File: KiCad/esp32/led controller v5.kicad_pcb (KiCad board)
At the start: 2 copper layers, 100 x 100 mm, 119 parts, among them J1 Conn_02x15_Counter_Clockwise, J10 Jack-DC, J13 i2c_3.3v, J2 charger, J3 Screw_Terminal_01x09, J4 Screw_Terminal_01x04, J5 Screw_Terminal_01x08, J6 OLED, J7 inverter, J8 i2c_5v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

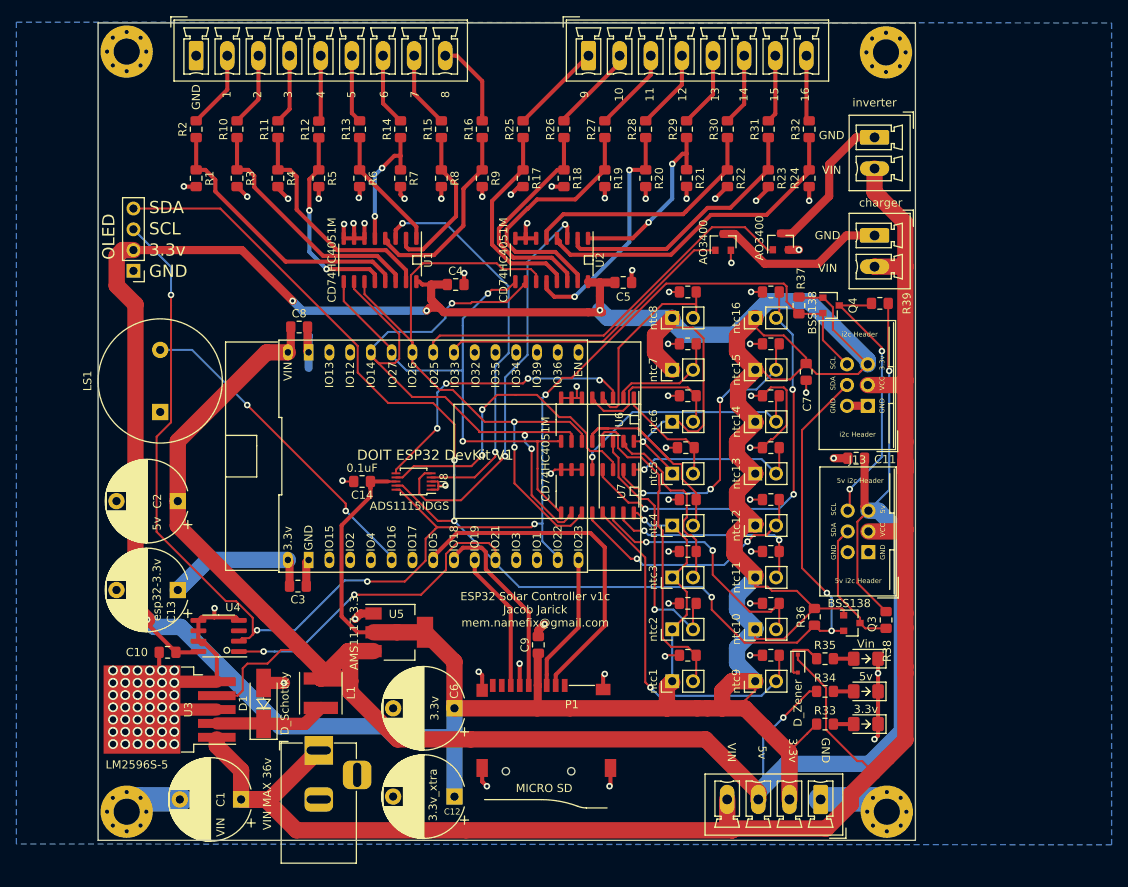
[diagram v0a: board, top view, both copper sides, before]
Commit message: updated ESP32 board
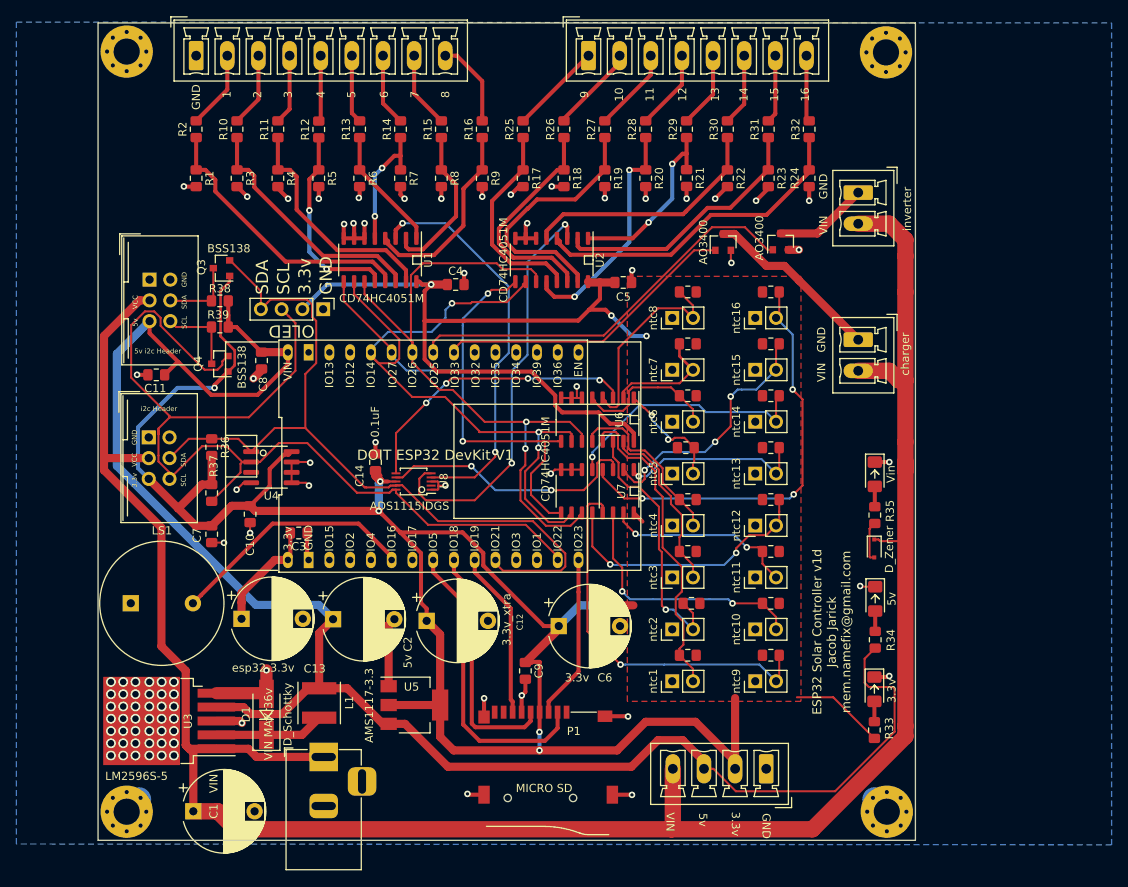
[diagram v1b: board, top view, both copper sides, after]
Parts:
- moved J8 94.1 mm to (7.30, 40.4), turned to 0 degrees
- moved R38 90.4 mm to (15.9, 43.0), turned to 0 degrees
- moved Q3 88.5 mm to (16.1, 39.0), turned to 180 degrees
- moved J13 88.1 mm to (7.20, 59.7), turned to 0 degrees
- moved C11 86.2 mm to (8.12, 52.0)
- moved R39 80.8 mm to (15.9, 46.2)
- moved R36 76.6 mm to (14.9, 60.9), turned to 270 degrees
- moved R37 75.4 mm to (14.9, 66.5)
- moved C7 75.4 mm to (14.9, 71.5)
- moved Q4 75.1 mm to (15.9, 50.7), turned to 180 degrees
- moved C2 23.9 mm to (29.8, 82.0), turned to 0 degrees
- moved J6 23.7 mm to (28.5, 44.0), turned to 270 degrees
- moved LS1 23.7 mm to (5.00, 80.0), turned to 0 degrees
- moved D5 22.6 mm to (96.0, 64.2), turned to 270 degrees
- moved C12 21.8 mm to (41.2, 82.2), turned to 0 degrees
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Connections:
- R40 pad 1: GND -> +3V3
- R41 pad 1: GND -> +3V3
- R42 pad 1: GND -> +3V3
- R43 pad 1: GND -> +3V3
- R44 pad 1: GND -> +3V3
- R45 pad 1: GND -> +3V3
- R46 pad 1: GND -> +3V3
- R47 pad 1: GND -> +3V3
- R48 pad 1: GND -> +3V3
- R49 pad 1: GND -> +3V3
- R50 pad 1: GND -> +3V3
- R51 pad 1: GND -> +3V3
- R52 pad 1: GND -> +3V3
- R53 pad 1: GND -> +3V3
- R54 pad 1: GND -> +3V3
- R55 pad 1: GND -> +3V3
- ntc1 pad 1: +3V3 -> GND
- ntc10 pad 1: +3V3 -> GND
- ntc11 pad 1: +3V3 -> GND
- ntc12 pad 1: +3V3 -> GND
- ntc13 pad 1: +3V3 -> GND
- ntc14 pad 1: +3V3 -> GND
- ntc15 pad 1: +3V3 -> GND
- ntc16 pad 1: +3V3 -> GND
- ntc2 pad 1: +3V3 -> GND
- ntc3 pad 1: +3V3 -> GND
- ntc4 pad 1: +3V3 -> GND
- ntc5 pad 1: +3V3 -> GND
- ntc6 pad 1: +3V3 -> GND
- ntc7 pad 1: +3V3 -> GND
- ntc8 pad 1: +3V3 -> GND
- ntc9 pad 1: +3V3 -> GND
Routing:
- net +3V3: track 553.3 -> 345.0 mm, vias 6 -> 9
- net io21: track 202.4 -> 99.4 mm, vias 7 -> 0
- net GND: track 200.4 -> 130.9 mm, vias 99 -> 87
- net vin: track 217.1 -> 272.0 mm
- net io22: track 180.4 -> 129.4 mm, vias 5 -> 0
- net +5V: track 259.4 -> 215.6 mm, vias 2 -> 0
- net scl5v: track 33.1 -> 9.84 mm, vias 2 -> 0
- net CH20: track 30.9 -> 21.4 mm
- net io16: track 40.2 -> 30.9 mm, vias 2 -> 0
- net AMUX4: track 39.3 -> 31.8 mm
- net sda5v: track 16.3 -> 9.15 mm
- net Net-(J7-Pad1): track 18.7 -> 11.6 mm
- net io18: track 23.5 -> 29.7 mm
- net io5: track 42.7 -> 36.6 mm
- net CH31: track 35.7 -> 31.2 mm
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- added copper zone on F.Cu, net +3V3
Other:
- board text added: "ESP32 Solar Controller v1d Jacob Jarick mem.namefix@gmail.com"
- board text removed: "ESP32 Solar Controller v1c Jacob Jarick mem.namefix@gmail.com"
